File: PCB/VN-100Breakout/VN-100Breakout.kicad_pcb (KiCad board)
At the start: 4 copper layers, 2 parts, among them U1 VN-100_Breakout, U2 VN-100

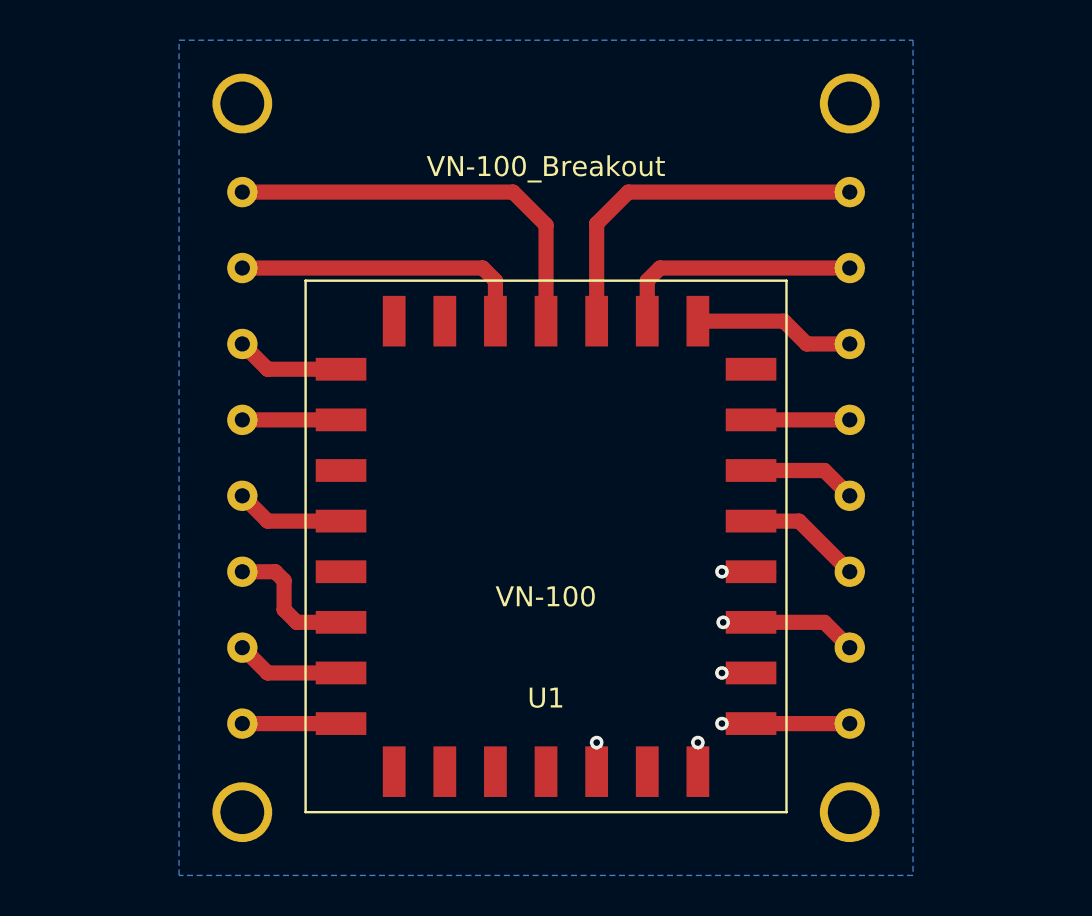
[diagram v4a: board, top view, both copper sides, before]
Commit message: file system modifications for multi user work and created vn-100 breakout step
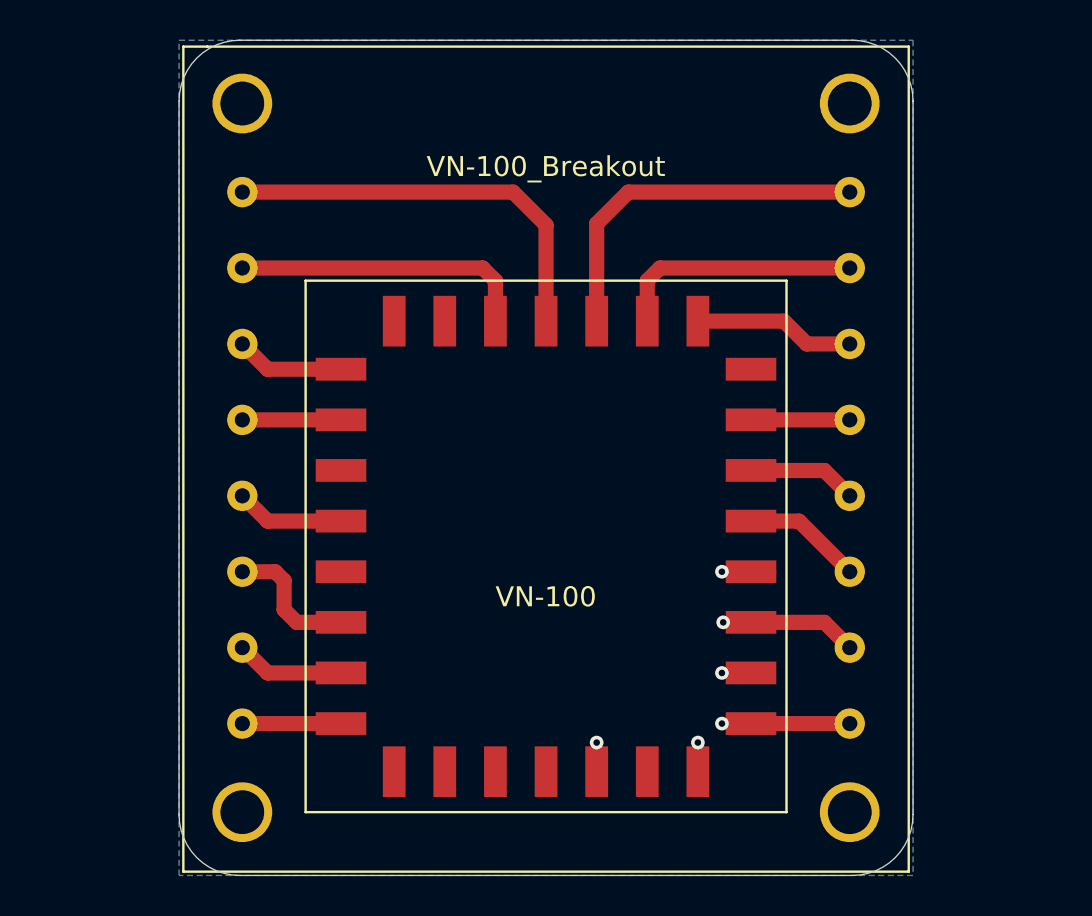
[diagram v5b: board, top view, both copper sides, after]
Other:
- board outline added: 36.8 x 41.9 mm
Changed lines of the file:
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@@
-(kicad_pcb (version 20171130) (host pcbnew "(5.1.10)-1")
+(kicad_pcb (version 20171130) (host pcbnew "(5.1.9)-1")
   (general
     (thickness 1.6002)
-    (drawings 1)
+    (drawings 9)
     (tracks 60)
     (zones 0)
@@
   )
   (setup
-    (last_trace_width 0.762)
+    (last_trace_width 0.254)
     (user_trace_width 0.127)
     (user_trace_width 0.254)
@@
       (effects (font (size 1 1) (thickness 0.15)))
     )
-    (fp_line (start 12.192 -13.462) (end -12.192 -13.462) (layer F.CrtYd) (width 0.12))
-    (fp_line (start 12.192 13.462) (end -12.192 13.462) (layer F.CrtYd) (width 0.12))
-    (fp_line (start 12.192 -13.462) (end 12.192 13.462) (layer F.CrtYd) (width 0.12))
-    (fp_line (start -12.192 13.462) (end -12.192 -13.462) (layer F.CrtYd) (width 0.12))
+    (fp_poly (pts (xy 0.2 0.2) (xy -0.2 0.2) (xy -0.2 -0.2) (xy 0.2 -0.2)) (layer F.CrtYd) (width 0.1))
     (fp_line (start -12.065 -13.335) (end 12.065 -13.335) (layer F.SilkS) (width 0.12))
     (fp_line (start 12.065 -13.335) (end 12.065 13.335) (layer F.SilkS) (width 0.12))
@@
     (pad 9 smd rect (at 7.62 -11.303) (size 1.143 2.54) (layers Front F.Paste F.Mask)
       (net 11 /SYNC_OUT))
+    (model "C:/Users/raidr/Documents/Programming/LBR/Payload-2022-Electrical/PCB/Library/Step Files/vn100_smd.step"
+      (offset (xyz -11 -12 1))
+      (scale (xyz 1 1 1))
+      (rotate (xyz 0 180 90))
+    )
   )
   (module PayloadFootprints:VN-100Breakout (layer Front)
     (at 153.67 99.06)
-    (fp_text reference U1 (at 0 12.7) (layer F.SilkS)
+    (fp_text reference U1 (at 0 12.7) (layer F.SilkS) hide
       (effects (font (size 1 1) (thickness 0.15)))
     )
@@
       (effects (font (size 1 1) (thickness 0.15)))
     )
-    (fp_line (start -17.145 20.32) (end -17.145 -19.05) (layer F.CrtYd) (width 0.12))
-    (fp_line (start 15.875 20.32) (end -15.875 20.32) (layer F.CrtYd) (width 0.12))
-    (fp_line (start 17.145 -19.05) (end 17.145 20.32) (layer F.CrtYd) (width 0.12))
-    (fp_line (start -15.875 -19.05) (end 15.875 -19.05) (layer F.CrtYd) (width 0.12))
-    (fp_line (start -15.875 20.32) (end -17.145 20.32) (layer F.CrtYd) (width 0.12))
-    (fp_line (start 15.875 20.32) (end 17.145 20.32) (layer F.CrtYd) (width 0.12))
-    (fp_line (start 15.875 -19.05) (end 17.145 -19.05) (layer F.CrtYd) (width 0.12))
-    (fp_line (start -15.875 -19.05) (end -17.145 -19.05) (layer F.CrtYd) (width 0.12))
+    (fp_line (start -18.2 -20) (end -17 -20) (layer F.SilkS) (width 0.12))
+    (fp_line (start -18.2 21.4) (end -18.2 -20) (layer F.SilkS) (width 0.12))
+    (fp_line (start 18.2 21.4) (end -18.2 21.4) (layer F.SilkS) (width 0.12))
+    (fp_line (start 18.2 -20) (end 18.2 21.4) (layer F.SilkS) (width 0.12))
+    (fp_line (start -17 -20) (end 18.2 -20) (layer F.SilkS) (width 0.12))
+    (fp_poly (pts (xy 2 12.3) (xy -1.9 12.3) (xy -1.9 9) (xy 2 9)) (layer F.CrtYd) (width 0.1))
     (pad "" thru_hole circle (at -15.24 18.415) (size 3 3) (drill 2.2) (layers *.Cu *.Mask))
     (pad "" thru_hole circle (at 15.24 18.415) (size 3 3) (drill 2.2) (layers *.Cu *.Mask))
@@
       (net 1 /SPI_MOSI))
   )
+  (gr_arc (start 169.037 81.788) (end 172.085 81.788) (angle -90) (layer Edge.Cuts) (width 0.0381))
+  (gr_arc (start 138.303 81.788) (end 138.303 78.74) (angle -90) (layer Edge.Cuts) (width 0.0381))
+  (gr_arc (start 138.303 117.602) (end 135.255 117.602) (angle -90) (layer Edge.Cuts) (width 0.0381))
+  (gr_arc (start 169.037 117.602) (end 169.037 120.65) (angle -90) (layer Edge.Cuts) (width 0.0381))
+  (gr_line (start 172.085 81.788) (end 172.085 117.602) (layer Edge.Cuts) (width 0.0381))
+  (gr_line (start 138.303 78.74) (end 169.037 78.74) (layer Edge.Cuts) (width 0.0381))
+  (gr_line (start 135.255 117.602) (end 135.255 81.788) (layer Edge.Cuts) (width 0.0381))
+  (gr_line (start 169.037 120.65) (end 138.303 120.65) (layer Edge.Cuts) (width 0.0381))
   (gr_line (start 151.13 93.98) (end 151.13 93.345) (layer Cmts.User) (width 0.1524))
   (segment (start 143.383 97.79) (end 143.383 97.917) (width 0.254) (layer Front) (net 1) (status 30))

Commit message: Changed VN-100 Breakout
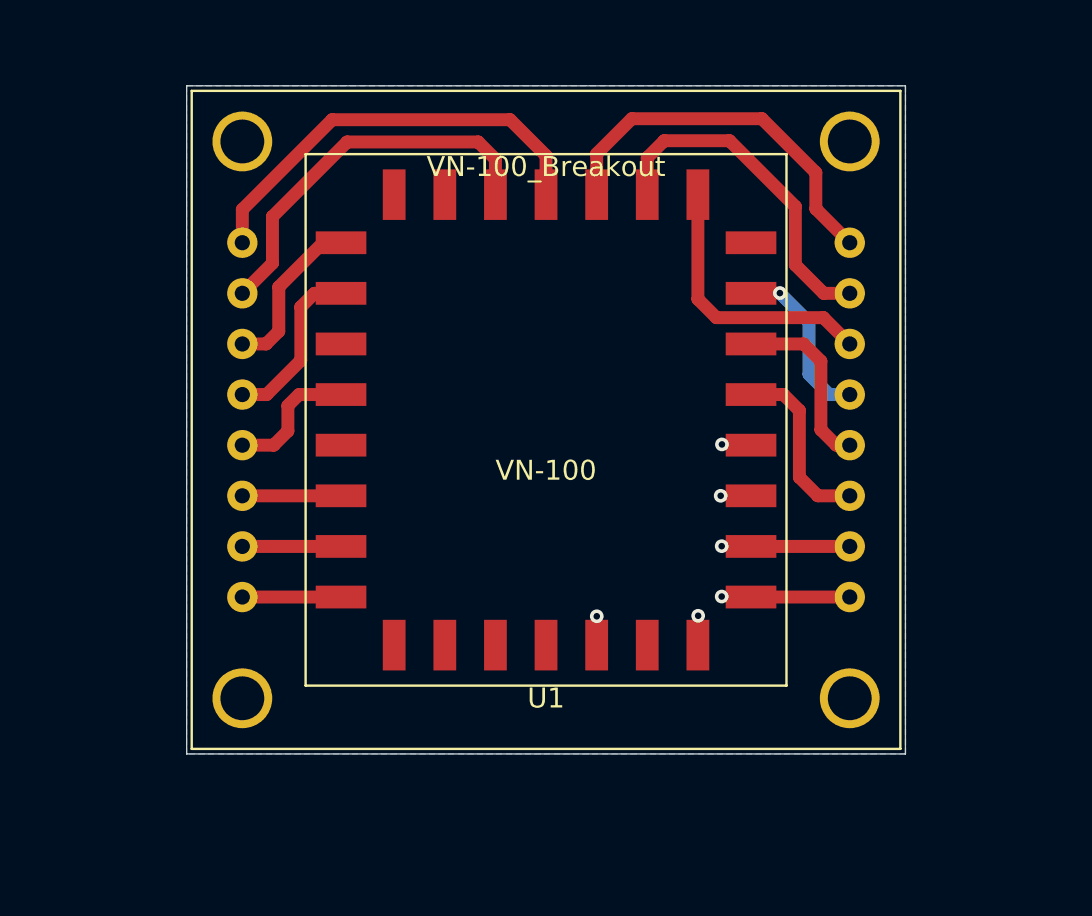
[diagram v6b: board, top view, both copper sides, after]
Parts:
- U1: footprint PayloadFootprints:VN-100Breakout -> VN-100Breakout:VN-100Breakout
- moved U2 6.35 mm to (153.7, 97.8)
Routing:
- net /SYNC_OUT: track 8.27 -> 13.8 mm
- net /RX1: track 15.1 -> 19.4 mm
- net /Vin: track 13.2 -> 17.3 mm
- net /SPI_MOSI: track 5.08 -> 8.63 mm
- net /SPI_SCK: track 5.48 -> 8.36 mm
- net /TX2: track 6.62 -> 9.07 mm
- net /Restore: track 6.22 -> 8.60 mm, vias 0 -> 1
- net /NRST: track 7.11 -> 4.95 mm
- net /RX2: track 6.89 -> 9.02 mm
- net /GND: track 20.6 -> 18.8 mm
- net /SPI_MISO: track 5.48 -> 6.96 mm
- net /Enable: track 18.2 -> 19.1 mm
- net /TX1: track 20.7 -> 21.5 mm
- net /SYNC_IN: track 5.48 -> 4.95 mm
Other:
- board size 36.8 x 41.9 mm -> 36.1 x 33.5 mm

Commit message: fixed vn-100 layer count and fill
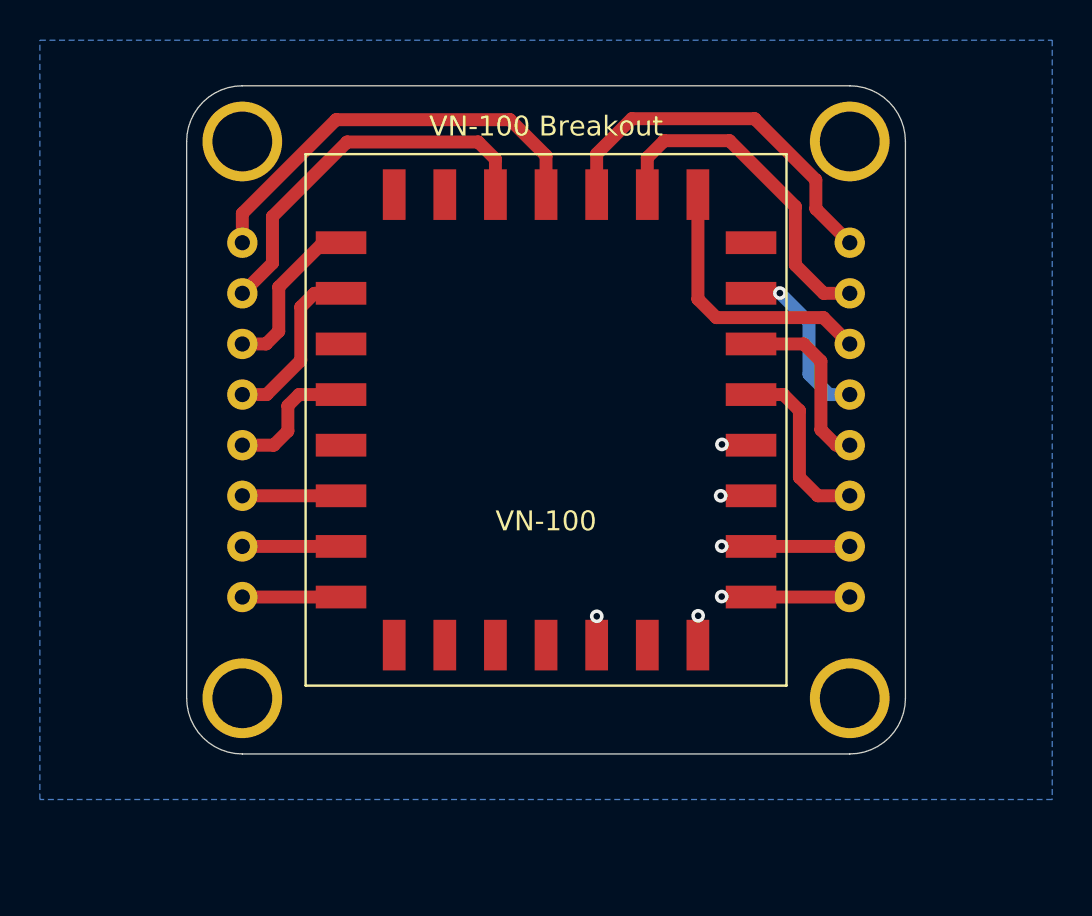
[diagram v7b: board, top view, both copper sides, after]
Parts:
- U1: value VN-100_Breakout -> VN-100 Breakout
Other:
- outline, holes or cut-outs redrawn
- copper layers 4 -> 2
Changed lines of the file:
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@@
-(kicad_pcb (version 20171130) (host pcbnew "(5.1.10)-1")
+(kicad_pcb (version 20171130) (host pcbnew "(5.1.9)-1")
   (general
     (thickness 1.6002)
-    (drawings 5)
+    (drawings 11)
     (tracks 83)
     (zones 0)
@@
   (layers
     (0 Front signal)
-    (1 In1.Cu signal)
-    (2 In2.Cu signal)
     (31 Back signal)
     (34 B.Paste user)
@@
   )
   (setup
-    (last_trace_width 0.508)
+    (last_trace_width 0.254)
     (user_trace_width 0.127)
     (user_trace_width 0.254)
@@
   (module VN-100Breakout:VN-100Breakout (layer Front)
     (at 153.67 99.06)
-    (fp_text reference U1 (at 0 12.7) (layer F.SilkS)
+    (fp_text reference U1 (at 0 -0.508) (layer F.SilkS) hide
       (effects (font (size 1 1) (thickness 0.15)))
     )
-    (fp_text value VN-100_Breakout (at 0 -13.97) (layer F.SilkS)
+    (fp_text value "VN-100 Breakout" (at 0 -16.002) (layer F.SilkS)
       (effects (font (size 1 1) (thickness 0.15)))
     )
-    (fp_line (start -17.78 -17.78) (end 17.78 -17.78) (layer F.SilkS) (width 0.12))
-    (fp_line (start -17.78 15.24) (end -17.78 -17.78) (layer F.SilkS) (width 0.12))
-    (fp_line (start 17.78 15.24) (end -17.78 15.24) (layer F.SilkS) (width 0.12))
-    (fp_line (start 17.78 -17.78) (end 17.78 15.24) (layer F.SilkS) (width 0.12))
-    (fp_poly (pts (xy 2 12.3) (xy -1.9 12.3) (xy -1.9 9) (xy 2 9)) (layer F.CrtYd) (width 0.1))
-    (pad "" thru_hole circle (at -15.24 12.7) (size 3 3) (drill 2.2) (layers *.Cu *.Mask))
-    (pad "" thru_hole circle (at 15.24 12.7) (size 3 3) (drill 2.2) (layers *.Cu *.Mask))
-    (pad "" thru_hole circle (at 15.24 -15.24 180) (size 3 3) (drill 2.2) (layers *.Cu *.Mask))
-    (pad "" thru_hole circle (at -15.24 -15.24) (size 3 3) (drill 2.2) (layers *.Cu *.Mask))
+    (fp_poly (pts (xy 2 5.84) (xy -1.9 5.84) (xy -1.9 2.54) (xy 2 2.54)) (layer F.CrtYd) (width 0.1))
+    (fp_line (start 17.78 -17.78) (end -17.78 -17.78) (layer Dwgs.User) (width 0.12))
+    (fp_line (start -17.78 -17.78) (end -17.78 15.24) (layer Dwgs.User) (width 0.12))
+    (fp_line (start -17.78 15.24) (end 17.78 15.24) (layer Dwgs.User) (width 0.12))
+    (fp_line (start 17.78 15.24) (end 17.78 -17.78) (layer Dwgs.User) (width 0.12))
+    (pad "" thru_hole circle (at -15.24 12.7) (size 4 4) (drill 3) (layers *.Cu *.Mask))
+    (pad "" thru_hole circle (at 15.24 12.7) (size 4 4) (drill 3) (layers *.Cu *.Mask))
+    (pad "" thru_hole circle (at 15.24 -15.24 180) (size 4 4) (drill 3) (layers *.Cu *.Mask))
+    (pad "" thru_hole circle (at -15.24 -15.24) (size 4 4) (drill 3) (layers *.Cu *.Mask))
     (pad 12 thru_hole circle (at 15.24 0) (size 1.524 1.524) (drill 0.762) (layers *.Cu *.Mask)
       (net 14 /TX2))
@@
       (effects (font (size 1 1) (thickness 0.15)))
     )
-    (fp_text value VN-100 (at 0 2.54) (layer F.SilkS)
+    (fp_text value VN-100 (at 0 5.08) (layer F.SilkS)
       (effects (font (size 1 1) (thickness 0.15)))
     )
+    (fp_line (start -12.065 13.335) (end -12.065 -13.335) (layer F.SilkS) (width 0.12))
+    (fp_line (start 12.065 13.335) (end -12.065 13.335) (layer F.SilkS) (width 0.12))
+    (fp_line (start 12.065 -13.335) (end 12.065 13.335) (layer F.SilkS) (width 0.12))
+    (fp_line (start -12.065 -13.335) (end 12.065 -13.335) (layer F.SilkS) (width 0.12))
+    (fp_line (start -12.192 13.462) (end -12.192 -13.462) (layer F.CrtYd) (width 0.12))
+    (fp_line (start 12.192 -13.462) (end 12.192 13.462) (layer F.CrtYd) (width 0.12))
+    (fp_line (start 12.192 13.462) (end -12.192 13.462) (layer F.CrtYd) (width 0.12))
     (fp_line (start 12.192 -13.462) (end -12.192 -13.462) (layer F.CrtYd) (width 0.12))
-    (fp_line (start 12.192 13.462) (end -12.192 13.462) (layer F.CrtYd) (width 0.12))
-    (fp_line (start 12.192 -13.462) (end 12.192 13.462) (layer F.CrtYd) (width 0.12))
-    (fp_line (start -12.192 13.462) (end -12.192 -13.462) (layer F.CrtYd) (width 0.12))
-    (fp_line (start -12.065 -13.335) (end 12.065 -13.335) (layer F.SilkS) (width 0.12))
-    (fp_line (start 12.065 -13.335) (end 12.065 13.335) (layer F.SilkS) (width 0.12))
-    (fp_line (start 12.065 13.335) (end -12.065 13.335) (layer F.SilkS) (width 0.12))
-    (fp_line (start -12.065 13.335) (end -12.065 -13.335) (layer F.SilkS) (width 0.12))
     (pad 16 smd rect (at -10.287 -8.89 90) (size 1.143 2.54) (layers Front F.Paste F.Mask)
       (net 4 /SPI_SCK))
@@
       (net 11 /SYNC_OUT))
   )
-  (gr_line (start 171.704 81.026) (end 135.636 81.026) (layer Edge.Cuts) (width 0.0381))
-  (gr_line (start 171.704 114.554) (end 171.704 81.026) (layer Edge.Cuts) (width 0.0381))
-  (gr_line (start 135.636 114.554) (end 171.704 114.554) (layer Edge.Cuts) (width 0.0381))
-  (gr_line (start 135.636 81.026) (end 135.636 114.554) (layer Edge.Cuts) (width 0.0381))
+  (gr_poly (pts (xy 179.07 116.84) (xy 128.27 116.84) (xy 128.27 78.74) (xy 179.07 78.74)) (layer Cmts.User) (width 0.1))
+  (gr_poly (pts (xy 179.07 116.84) (xy 128.27 116.84) (xy 128.27 78.74) (xy 179.07 78.74)) (layer Cmts.User) (width 0.1))
+  (gr_arc (start 138.43 83.82) (end 138.43 81.026) (angle -90) (layer Edge.Cuts) (width 0.0381))
+  (gr_arc (start 138.43 111.76) (end 135.636 111.76) (angle -90) (layer Edge.Cuts) (width 0.0381))
+  (gr_arc (start 168.91 111.76) (end 168.91 114.554) (angle -90) (layer Edge.Cuts) (width 0.0381))
+  (gr_arc (start 168.91 83.82) (end 171.704 83.82) (angle -90) (layer Edge.Cuts) (width 0.0381))
+  (gr_line (start 168.91 81.026) (end 138.43 81.026) (layer Edge.Cuts) (width 0.0381))
+  (gr_line (start 171.704 111.76) (end 171.704 83.82) (layer Edge.Cuts) (width 0.0381))
+  (gr_line (start 138.43 114.554) (end 168.91 114.554) (layer Edge.Cuts) (width 0.0381))
+  (gr_line (start 135.636 83.82) (end 135.636 111.76) (layer Edge.Cuts) (width 0.0381))
   (gr_line (start 151.13 93.98) (end 151.13 93.345) (layer Cmts.User) (width 0.1524))
   (segment (start 141.3637 94.8055) (end 139.6492 96.52) (width 0.65) (layer Front) (net 1))
@@
   (segment (start 142.4813 88.9) (end 140.2588 91.1225) (width 0.65) (layer Front) (net 4))
   (segment (start 143.383 88.9) (end 142.4813 88.9) (width 0.65) (layer Front) (net 4))
+  (segment (start 153.67 84.5312) (end 153.67 86.487) (width 0.65) (layer Front) (net 5))
   (segment (start 151.8666 82.7278) (end 153.67 84.5312) (width 0.65) (layer Front) (net 5))
-  (segment (start 153.67 84.5312) (end 153.67 86.487) (width 0.65) (layer Front) (net 5))
-  (segment (start 142.9385 82.7278) (end 151.8666 82.7278) (width 0.65) (layer Front) (net 5))
-  (segment (start 138.43 87.2363) (end 142.9385 82.7278) (width 0.65) (layer Front) (net 5))
-  (segment (start 138.43 88.9) (end 138.43 87.2363) (width 0.65) (layer Front) (net 5))
+  (segment (start 143.13535 82.7278) (end 151.8666 82.7278) (width 0.65) (layer Front) (net 5))
+  (segment (start 138.43 87.43315) (end 143.13535 82.7278) (width 0.65) (layer Front) (net 5))
+  (segment (start 138.43 88.9) (end 138.43 87.43315) (width 0.65) (layer Front) (net 5))
   (segment (start 143.383 96.52) (end 143.167098 96.52) (width 0.762) (layer Front) (net 6))
   (segment (start 138.43 99.06) (end 140.0048 99.06) (width 0.65) (layer Front) (net 6))
@@
   (segment (start 156.21 84.4423) (end 156.21 86.487) (width 0.65) (layer Front) (net 9))
   (segment (start 157.9753 82.677) (end 156.21 84.4423) (width 0.65) (layer Front) (net 9))
-  (segment (start 164.5031 82.677) (end 157.9753 82.677) (width 0.65) (layer Front) (net 9))
-  (segment (start 167.2082 85.3821) (end 164.5031 82.677) (width 0.65) (layer Front) (net 9))
-  (segment (start 167.2082 87.1982) (end 167.2082 85.3821) (width 0.65) (layer Front) (net 9))
+  (segment (start 164.138038 82.677) (end 157.9753 82.677) (width 0.65) (layer Front) (net 9))
+  (segment (start 167.2082 85.747162) (end 164.138038 82.677) (width 0.65) (layer Front) (net 9))
+  (segment (start 167.2082 87.1982) (end 167.2082 85.747162) (width 0.65) (layer Front) (net 9))
   (segment (start 168.91 88.9) (end 167.2082 87.1982) (width 0.65) (layer Front) (net 9))
   (segment (start 159.6009 83.7819) (end 158.75 84.6328) (width 0.65) (layer Front) (net 10))
@@
   (segment (start 166.3827 97.3201) (end 166.3827 100.6729) (width 0.65) (layer Front) (net 15))
   (segment (start 165.5826 96.52) (end 166.3827 97.3201) (width 0.65) (layer Front) (net 15))
+  (zone (net 0) (net_name "") (layer Cmts.User) (hatch edge 0.508)
+    (connect_pads (clearance 0.508))
+    (min_thickness 0.254)
+    (fill yes (arc_segments 32) (thermal_gap 0.508) (thermal_bridge_width 0.508))
+    (polygon
+      (pts
+        (xy 179.07 116.84) (xy 128.27 116.84) (xy 128.27 78.74) (xy 179.07 78.74)
+      )
+    )
+  )
   (zone (net 13) (net_name /GND) (layer Back) (hatch edge 0.508)
     (connect_pads (clearance 0.508))
@@
     (polygon
       (pts
-        (xy 171.704 114.554) (xy 135.636 114.554) (xy 135.636 81.026) (xy 171.704 81.026)
+        (xy 179.07 116.84) (xy 128.27 116.84) (xy 128.27 78.74) (xy 179.07 78.74)
       )
     )
